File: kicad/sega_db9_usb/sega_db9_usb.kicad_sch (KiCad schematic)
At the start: 7 parts

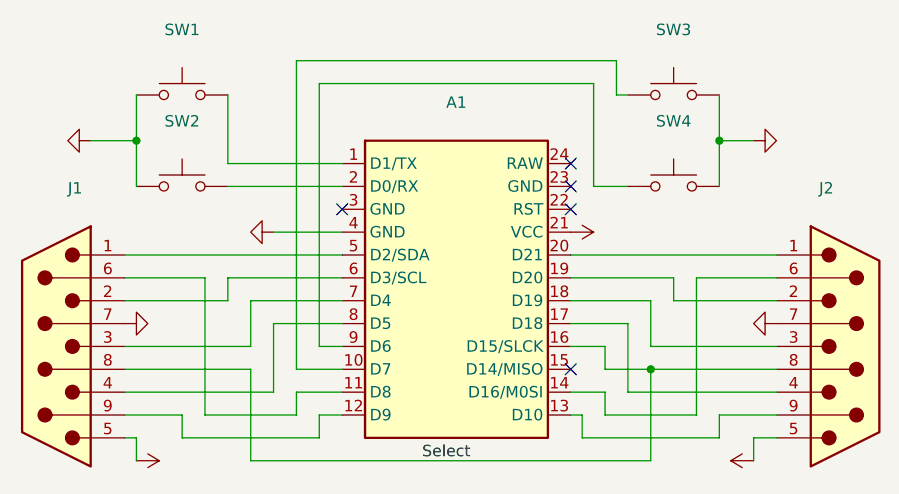
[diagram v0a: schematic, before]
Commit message: bug pins 8 and 7
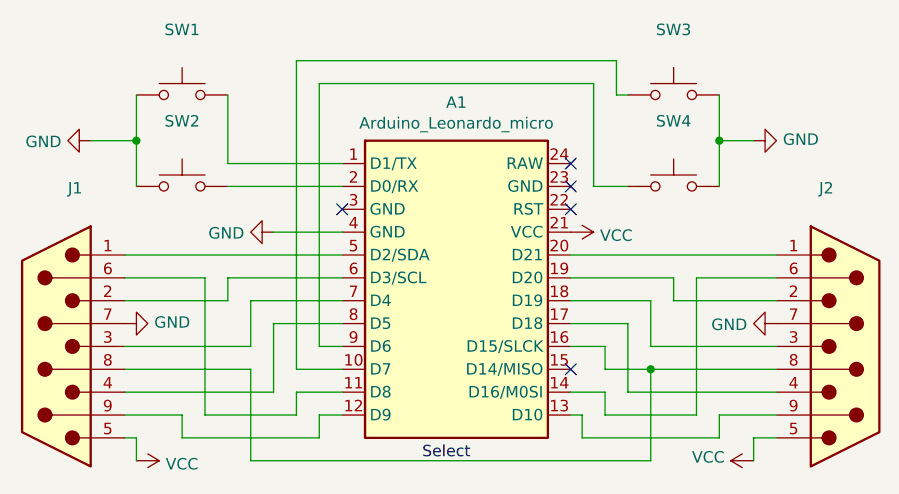
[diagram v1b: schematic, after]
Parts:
- A1: value (none) -> Arduino_Leonardo_micro; footprint (none) -> Module:Arduino_UNO_R3
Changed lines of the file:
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@@
     (in_bom yes) (on_board yes)
     (property "Reference" "A1" (id 0) (at 137.16 54.1782 0))
-    (property "Value" "" (id 1) (at 137.16 56.4896 0))
-    (property "Footprint" "" (id 2) (at 137.16 81.28 0)
+    (property "Value" "Arduino_Leonardo_micro" (id 1) (at 137.16 56.4896 0))
+    (property "Footprint" "Module:Arduino_UNO_R3" (id 2) (at 137.16 81.28 0)
       (effects (font (size 1.27 1.27) italic) hide)
     )
@@
       (effects (font (size 1.27 1.27)) hide)
     )
-    (property "Value" "" (id 1) (at 104.8512 94.361 90)
+    (property "Value" "VCC" (id 1) (at 104.8512 94.361 90)
       (effects (font (size 1.27 1.27)) (justify left))
     )
@@
       (effects (font (size 1.27 1.27)) hide)
     )
-    (property "Value" "" (id 1) (at 166.9542 93.599 90)
+    (property "Value" "VCC" (id 1) (at 166.9542 93.599 90)
       (effects (font (size 1.27 1.27)) (justify left))
     )
@@
       (effects (font (size 1.27 1.27)) hide)
     )
-    (property "Value" "" (id 1) (at 103.5812 78.613 90)
+    (property "Value" "GND" (id 1) (at 103.5812 78.613 90)
       (effects (font (size 1.27 1.27)) (justify right))
     )
@@
       (effects (font (size 1.27 1.27)) hide)
     )
-    (property "Value" "" (id 1) (at 169.4688 78.867 90)
+    (property "Value" "GND" (id 1) (at 169.4688 78.867 90)
       (effects (font (size 1.27 1.27)) (justify right))
     )
@@
       (effects (font (size 1.27 1.27)) hide)
     )
-    (property "Value" "" (id 1) (at 153.1112 68.961 90)
+    (property "Value" "VCC" (id 1) (at 153.1112 68.961 90)
       (effects (font (size 1.27 1.27)) (justify left))
     )
@@
       (effects (font (size 1.27 1.27)) hide)
     )
-    (property "Value" "" (id 1) (at 113.5888 68.707 90)
+    (property "Value" "GND" (id 1) (at 113.5888 68.707 90)
       (effects (font (size 1.27 1.27)) (justify right))
     )
@@
       (effects (font (size 1.27 1.27)) hide)
     )
-    (property "Value" "" (id 1) (at 173.4312 58.293 90)
+    (property "Value" "GND" (id 1) (at 173.4312 58.293 90)
       (effects (font (size 1.27 1.27)) (justify right))
     )
@@
       (effects (font (size 1.27 1.27)) hide)
     )
-    (property "Value" "" (id 1) (at 93.2688 58.547 90)
+    (property "Value" "GND" (id 1) (at 93.2688 58.547 90)
       (effects (font (size 1.27 1.27)) (justify right))
     )
@@
     )
     (path "/00000000-0000-0000-0000-00006243830a"
-      (reference "J1") (unit 1) (value "DB9_Male") (footprint "")
+      (reference "J1") (unit 1) (value "Player 1") (footprint "")
     )
     (path "/00000000-0000-0000-0000-000062438ff1"
-      (reference "J2") (unit 1) (value "DB9_Male") (footprint "")
+      (reference "J2") (unit 1) (value "Player 2") (footprint "")
     )
     (path "/00000000-0000-0000-0000-0000624736be"
-      (reference "SW1") (unit 1) (value "SW_Push") (footprint "")
+      (reference "SW1") (unit 1) (value "Select") (footprint "")
     )
     (path "/00000000-0000-0000-0000-0000624746c1"
-      (reference "SW2") (unit 1) (value "SW_Push") (footprint "")
+      (reference "SW2") (unit 1) (value "Y") (footprint "")
     )
     (path "/00000000-0000-0000-0000-0000624771b2"
-      (reference "SW3") (unit 1) (value "SW_Push") (footprint "")
+      (reference "SW3") (unit 1) (value "Select") (footprint "")
     )
     (path "/00000000-0000-0000-0000-00006247909a"
-      (reference "SW4") (unit 1) (value "SW_Push") (footprint "")
-    )
-  )
+      (reference "SW4") (unit 1) (value "Y") (footprint "")
+    )
+  )

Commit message: Wroking
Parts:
- J1: value (none) -> Player 1
- J2: value (none) -> Player 2
- SW1, SW3: value (none) -> Select
- SW2, SW4: value (none) -> Y
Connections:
- net GND: now also J1.8, J2.8; no longer J1.7, J2.7
- net Select: now also J1.7, J2.7; no longer J1.8, J2.8
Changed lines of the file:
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@@
   (junction (at 166.37 58.42) (diameter 0) (color 0 0 0 0)
   )
-  (junction (at 158.75 83.82) (diameter 0) (color 0 0 0 0)
-  )
   (junction (at 101.6 58.42) (diameter 0) (color 0 0 0 0)
+  )
+  (junction (at 161.29 83.82) (diameter 0) (color 0 0 0 0)
   )
   (no_connect (at 149.86 66.04))
@@
   (no_connect (at 149.86 60.96))
   (no_connect (at 124.46 66.04))
+  (wire (pts (xy 161.29 78.74) (xy 172.72 78.74))
+    (stroke (width 0) (type default) (color 0 0 0 0))
+  )
   (wire (pts (xy 158.75 76.2) (xy 149.86 76.2))
     (stroke (width 0) (type default) (color 0 0 0 0))
@@
     (stroke (width 0) (type default) (color 0 0 0 0))
   )
-  (wire (pts (xy 158.75 83.82) (xy 158.75 93.98))
+  (wire (pts (xy 161.29 83.82) (xy 161.29 93.98))
     (stroke (width 0) (type default) (color 0 0 0 0))
   )
@@
     (stroke (width 0) (type default) (color 0 0 0 0))
   )
+  (wire (pts (xy 100.33 78.74) (xy 111.76 78.74))
+    (stroke (width 0) (type default) (color 0 0 0 0))
+  )
   (wire (pts (xy 151.13 88.9) (xy 151.13 91.44))
     (stroke (width 0) (type default) (color 0 0 0 0))
@@
     (stroke (width 0) (type default) (color 0 0 0 0))
   )
-  (wire (pts (xy 158.75 93.98) (xy 114.3 93.98))
+  (wire (pts (xy 161.29 93.98) (xy 111.76 93.98))
     (stroke (width 0) (type default) (color 0 0 0 0))
   )
@@
     (stroke (width 0) (type default) (color 0 0 0 0))
   )
-  (wire (pts (xy 153.67 83.82) (xy 158.75 83.82))
-    (stroke (width 0) (type default) (color 0 0 0 0))
-  )
   (wire (pts (xy 153.67 81.28) (xy 153.67 83.82))
     (stroke (width 0) (type default) (color 0 0 0 0))
   )
-  (wire (pts (xy 158.75 83.82) (xy 172.72 83.82))
-    (stroke (width 0) (type default) (color 0 0 0 0))
-  )
   (wire (pts (xy 121.92 81.28) (xy 124.46 81.28))
     (stroke (width 0) (type default) (color 0 0 0 0))
@@
     (stroke (width 0) (type default) (color 0 0 0 0))
   )
+  (wire (pts (xy 111.76 78.74) (xy 111.76 93.98))
+    (stroke (width 0) (type default) (color 0 0 0 0))
+  )
   (wire (pts (xy 100.33 76.2) (xy 111.76 76.2))
     (stroke (width 0) (type default) (color 0 0 0 0))
@@
     (stroke (width 0) (type default) (color 0 0 0 0))
   )
-  (wire (pts (xy 114.3 83.82) (xy 100.33 83.82))
-    (stroke (width 0) (type default) (color 0 0 0 0))
-  )
   (wire (pts (xy 119.38 49.53) (xy 154.94 49.53))
     (stroke (width 0) (type default) (color 0 0 0 0))
@@
     (stroke (width 0) (type default) (color 0 0 0 0))
   )
+  (wire (pts (xy 153.67 83.82) (xy 161.29 83.82))
+    (stroke (width 0) (type default) (color 0 0 0 0))
+  )
   (wire (pts (xy 149.86 88.9) (xy 151.13 88.9))
     (stroke (width 0) (type default) (color 0 0 0 0))
   )
-  (wire (pts (xy 114.3 93.98) (xy 114.3 83.82))
+  (wire (pts (xy 161.29 83.82) (xy 161.29 78.74))
     (stroke (width 0) (type default) (color 0 0 0 0))
   )
@@
     (in_bom yes) (on_board yes)
     (property "Reference" "J1" (id 0) (at 94.7928 63.7032 0))
-    (property "Value" "" (id 1) (at 94.7928 66.0146 0))
+    (property "Value" "Player 1" (id 1) (at 94.7928 66.0146 0))
     (property "Footprint" "" (id 2) (at 92.71 81.28 0)
       (effects (font (size 1.27 1.27)) hide)
@@
     (in_bom yes) (on_board yes)
     (property "Reference" "J2" (id 0) (at 178.2572 63.7032 0))
-    (property "Value" "" (id 1) (at 178.2572 66.0146 0))
+    (property "Value" "Player 2" (id 1) (at 178.2572 66.0146 0))
     (property "Footprint" "" (id 2) (at 180.34 81.28 0)
       (effects (font (size 1.27 1.27)) hide)
@@
     (pin "1")
   )
-  (symbol (lib_id "power:GND") (at 100.33 78.74 90) (unit 1)
-    (in_bom yes) (on_board yes)
-    (property "Reference" "#PWR0103" (id 0) (at 106.68 78.74 0)
-      (effects (font (size 1.27 1.27)) hide)
-    )
-    (property "Value" "GND" (id 1) (at 103.5812 78.613 90)
+  (symbol (lib_id "power:GND") (at 100.33 83.82 90) (unit 1)
+    (in_bom yes) (on_board yes)
+    (property "Reference" "#PWR0103" (id 0) (at 106.68 83.82 0)
+      (effects (font (size 1.27 1.27)) hide)
+    )
+    (property "Value" "GND" (id 1) (at 103.5812 83.693 90)
       (effects (font (size 1.27 1.27)) (justify right))
     )
-    (property "Footprint" "" (id 2) (at 100.33 78.74 0)
-      (effects (font (size 1.27 1.27)) hide)
-    )
-    (property "Datasheet" "" (id 3) (at 100.33 78.74 0)
-      (effects (font (size 1.27 1.27)) hide)
-    )
-    (pin "1")
-  )
-  (symbol (lib_id "power:GND") (at 172.72 78.74 270) (unit 1)
-    (in_bom yes) (on_board yes)
-    (property "Reference" "#PWR0104" (id 0) (at 166.37 78.74 0)
-      (effects (font (size 1.27 1.27)) hide)
-    )
-    (property "Value" "GND" (id 1) (at 169.4688 78.867 90)
+    (property "Footprint" "" (id 2) (at 100.33 83.82 0)
+      (effects (font (size 1.27 1.27)) hide)
+    )
+    (property "Datasheet" "" (id 3) (at 100.33 83.82 0)
+      (effects (font (size 1.27 1.27)) hide)
+    )
+    (pin "1")
+  )
+  (symbol (lib_id "power:GND") (at 172.72 83.82 270) (unit 1)
+    (in_bom yes) (on_board yes)
+    (property "Reference" "#PWR0104" (id 0) (at 166.37 83.82 0)
+      (effects (font (size 1.27 1.27)) hide)
+    )
+    (property "Value" "GND" (id 1) (at 169.4688 83.947 90)
       (effects (font (size 1.27 1.27)) (justify right))
     )
-    (property "Footprint" "" (id 2) (at 172.72 78.74 0)
-      (effects (font (size 1.27 1.27)) hide)
-    )
-    (property "Datasheet" "" (id 3) (at 172.72 78.74 0)
+    (property "Footprint" "" (id 2) (at 172.72 83.82 0)
+      (effects (font (size 1.27 1.27)) hide)
+    )
+    (property "Datasheet" "" (id 3) (at 172.72 83.82 0)
       (effects (font (size 1.27 1.27)) hide)
     )
@@
     (in_bom yes) (on_board yes)
     (property "Reference" "SW1" (id 0) (at 106.68 46.101 0))
-    (property "Value" "" (id 1) (at 106.68 48.4124 0))
+    (property "Value" "Select" (id 1) (at 106.68 48.4124 0))
     (property "Footprint" "" (id 2) (at 106.68 48.26 0)
       (effects (font (size 1.27 1.27)) hide)
@@
     (in_bom yes) (on_board yes)
     (property "Reference" "SW2" (id 0) (at 106.68 56.261 0))
-    (property "Value" "" (id 1) (at 106.68 58.5724 0))
+    (property "Value" "Y" (id 1) (at 106.68 58.5724 0))
     (property "Footprint" "" (id 2) (at 106.68 58.42 0)
       (effects (font (size 1.27 1.27)) hide)
@@
     (in_bom yes) (on_board yes)
     (property "Reference" "SW3" (id 0) (at 161.29 46.101 0))
-    (property "Value" "" (id 1) (at 161.29 48.4124 0))
+    (property "Value" "Select" (id 1) (at 161.29 48.4124 0))
     (property "Footprint" "" (id 2) (at 161.29 48.26 0)
       (effects (font (size 1.27 1.27)) hide)
@@
     (in_bom yes) (on_board yes)
     (property "Reference" "SW4" (id 0) (at 161.29 56.261 0))
-    (property "Value" "" (id 1) (at 161.29 58.5724 0))
+    (property "Value" "Y" (id 1) (at 161.29 58.5724 0))
     (property "Footprint" "" (id 2) (at 161.29 58.42 0)
       (effects (font (size 1.27 1.27)) hide)

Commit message: 2 players
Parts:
- A1: footprint Module:Arduino_UNO_R3 -> (none)
- J1, J2: footprint (none) -> Connector_Dsub:DSUB-9_Female_EdgeMount_P2.77mm
- SW1, SW2, SW3, SW4: footprint (none) -> Button_Switch_THT:SW_PUSH-12mm
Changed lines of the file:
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@@
     (property "Reference" "J1" (id 0) (at 94.7928 63.7032 0))
     (property "Value" "Player 1" (id 1) (at 94.7928 66.0146 0))
-    (property "Footprint" "" (id 2) (at 92.71 81.28 0)
+    (property "Footprint" "Connector_Dsub:DSUB-9_Female_EdgeMount_P2.77mm" (id 2) (at 92.71 81.28 0)
       (effects (font (size 1.27 1.27)) hide)
     )
@@
     (property "Reference" "J2" (id 0) (at 178.2572 63.7032 0))
     (property "Value" "Player 2" (id 1) (at 178.2572 66.0146 0))
-    (property "Footprint" "" (id 2) (at 180.34 81.28 0)
+    (property "Footprint" "Connector_Dsub:DSUB-9_Female_EdgeMount_P2.77mm" (id 2) (at 180.34 81.28 0)
       (effects (font (size 1.27 1.27)) hide)
     )
@@
     (property "Reference" "A1" (id 0) (at 137.16 54.1782 0))
     (property "Value" "Arduino_Leonardo_micro" (id 1) (at 137.16 56.4896 0))
-    (property "Footprint" "Module:Arduino_UNO_R3" (id 2) (at 137.16 81.28 0)
+    (property "Footprint" "" (id 2) (at 137.16 81.28 0)
       (effects (font (size 1.27 1.27) italic) hide)
     )
@@
     (property "Reference" "SW1" (id 0) (at 106.68 46.101 0))
     (property "Value" "Select" (id 1) (at 106.68 48.4124 0))
-    (property "Footprint" "" (id 2) (at 106.68 48.26 0)
+    (property "Footprint" "Button_Switch_THT:SW_PUSH-12mm" (id 2) (at 106.68 48.26 0)
       (effects (font (size 1.27 1.27)) hide)
     )
@@
     (property "Reference" "SW2" (id 0) (at 106.68 56.261 0))
     (property "Value" "Y" (id 1) (at 106.68 58.5724 0))
-    (property "Footprint" "" (id 2) (at 106.68 58.42 0)
+    (property "Footprint" "Button_Switch_THT:SW_PUSH-12mm" (id 2) (at 106.68 58.42 0)
       (effects (font (size 1.27 1.27)) hide)
     )
@@
     (property "Reference" "SW3" (id 0) (at 161.29 46.101 0))
     (property "Value" "Select" (id 1) (at 161.29 48.4124 0))
-    (property "Footprint" "" (id 2) (at 161.29 48.26 0)
+    (property "Footprint" "Button_Switch_THT:SW_PUSH-12mm" (id 2) (at 161.29 48.26 0)
       (effects (font (size 1.27 1.27)) hide)
     )
@@
     (property "Reference" "SW4" (id 0) (at 161.29 56.261 0))
     (property "Value" "Y" (id 1) (at 161.29 58.5724 0))
-    (property "Footprint" "" (id 2) (at 161.29 58.42 0)
+    (property "Footprint" "Button_Switch_THT:SW_PUSH-12mm" (id 2) (at 161.29 58.42 0)
       (effects (font (size 1.27 1.27)) hide)
     )
@@
     )
     (path "/00000000-0000-0000-0000-000062443a08"
-      (reference "A1") (unit 1) (value "Arduino_Leonardo_micro") (footprint "Module:Arduino_UNO_R3")
+      (reference "A1") (unit 1) (value "Arduino_Leonardo_micro") (footprint "Symbol:ProMicro")
     )
     (path "/00000000-0000-0000-0000-00006243830a"
-      (reference "J1") (unit 1) (value "Player 1") (footprint "")
+      (reference "J1") (unit 1) (value "Player 1") (footprint "Connector_Dsub:DSUB-9_Female_EdgeMount_P2.77mm")
     )
     (path "/00000000-0000-0000-0000-000062438ff1"
-      (reference "J2") (unit 1) (value "Player 2") (footprint "")
+      (reference "J2") (unit 1) (value "Player 2") (footprint "Connector_Dsub:DSUB-9_Female_EdgeMount_P2.77mm")
     )
     (path "/00000000-0000-0000-0000-0000624736be"
-      (reference "SW1") (unit 1) (value "Select") (footprint "")
+      (reference "SW1") (unit 1) (value "Select") (footprint "Button_Switch_THT:SW_PUSH-12mm")
     )
     (path "/00000000-0000-0000-0000-0000624746c1"
-      (reference "SW2") (unit 1) (value "Y") (footprint "")
+      (reference "SW2") (unit 1) (value "Y") (footprint "Button_Switch_THT:SW_PUSH-12mm")
     )
     (path "/00000000-0000-0000-0000-0000624771b2"
-      (reference "SW3") (unit 1) (value "Select") (footprint "")
+      (reference "SW3") (unit 1) (value "Select") (footprint "Button_Switch_THT:SW_PUSH-12mm")
     )
     (path "/00000000-0000-0000-0000-00006247909a"
-      (reference "SW4") (unit 1) (value "Y") (footprint "")
-    )
-  )
+      (reference "SW4") (unit 1) (value "Y") (footprint "Button_Switch_THT:SW_PUSH-12mm")
+    )
+  )
